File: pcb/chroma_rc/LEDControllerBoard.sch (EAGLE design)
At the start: 38 parts, among them Q1 FDC653NSSOT6, Q10 FDC653NSSOT6, Q11 FDC653NSSOT6, Q12 FDC653NSSOT6, Q13 FDC653NSSOT6, Q14 FDC653NSSOT6, Q2 FDC653NSSOT6, Q3 FDC653NSSOT6, Q4 FDC653NSSOT6, Q5 FDC653NSSOT6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

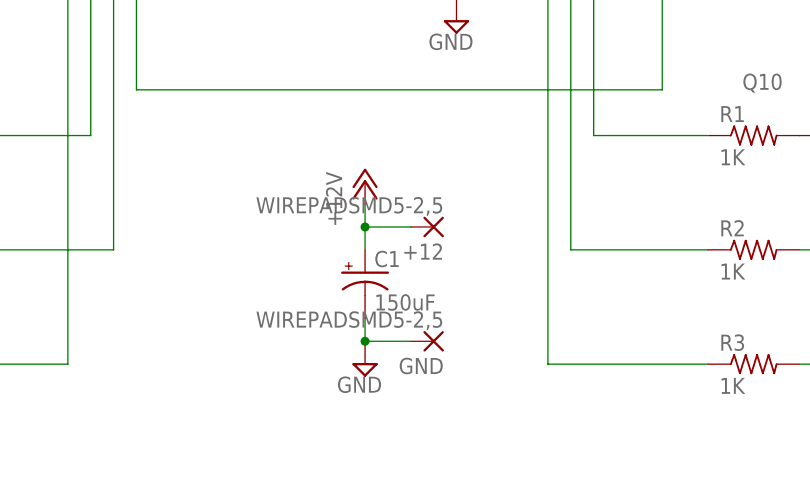
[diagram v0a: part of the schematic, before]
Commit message: PCB v1.3.  Added second set of power pads on the bottom.
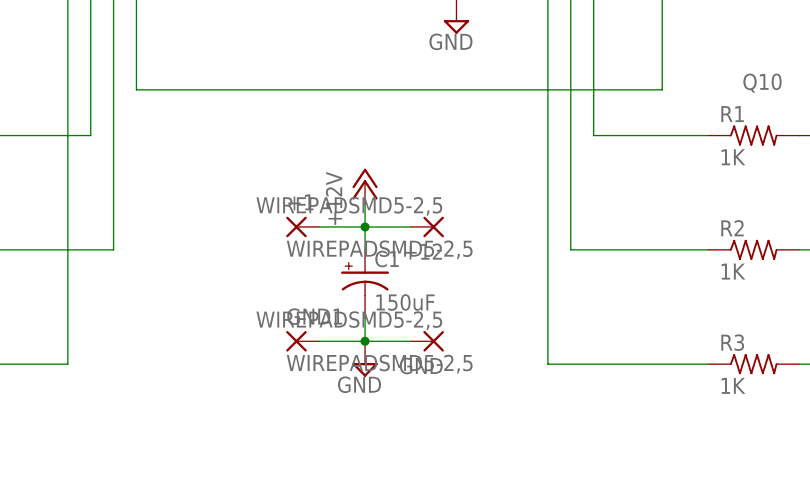
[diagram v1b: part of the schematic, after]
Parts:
- added +1, GND1: WIREPADSMD5-2,5, wirepad:WIREPADSMD5-2,5
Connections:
- net +12V: now also +1.P
- net GND: now also GND1.P
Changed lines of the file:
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@@
 <part name="P+4" library="supply1" deviceset="VCC" device=""/>
 <part name="C1" library="rcl" deviceset="CPOL-US" device="D" value="150uF"/>
+<part name="+1" library="wirepad" deviceset="WIREPAD" device="SMD5-2,5"/>
+<part name="GND1" library="wirepad" deviceset="WIREPAD" device="SMD5-2,5"/>
 </parts>
 <sheets>
@@
 <instance part="P+4" gate="VCC" x="5.08" y="127"/>
 <instance part="C1" gate="G$1" x="38.1" y="7.62"/>
+<instance part="+1" gate="G$1" x="30.48" y="12.7"/>
+<instance part="GND1" gate="G$1" x="30.48" y="0"/>
 </instances>
 <busses>
@@
 <wire x1="38.1" y1="0" x2="38.1" y2="2.54" width="0.1524" layer="91"/>
 <junction x="38.1" y="0"/>
+<pinref part="GND1" gate="G$1" pin="P"/>
+<wire x1="33.02" y1="0" x2="38.1" y2="0" width="0.1524" layer="91"/>
 </segment>
 <segment>
@@
 <wire x1="38.1" y1="10.16" x2="38.1" y2="12.7" width="0.1524" layer="91"/>
 <junction x="38.1" y="12.7"/>
-</segment>
-<segment>
+<pinref part="+1" gate="G$1" pin="P"/>
+<wire x1="33.02" y1="12.7" x2="38.1" y2="12.7" width="0.1524" layer="91"/>
+</segment>
+<segment>
